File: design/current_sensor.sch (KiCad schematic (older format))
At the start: 10 parts, among them J1 DS conn, J2 DS conn, J3 Conn, J4 DS conn, U1 Buffer

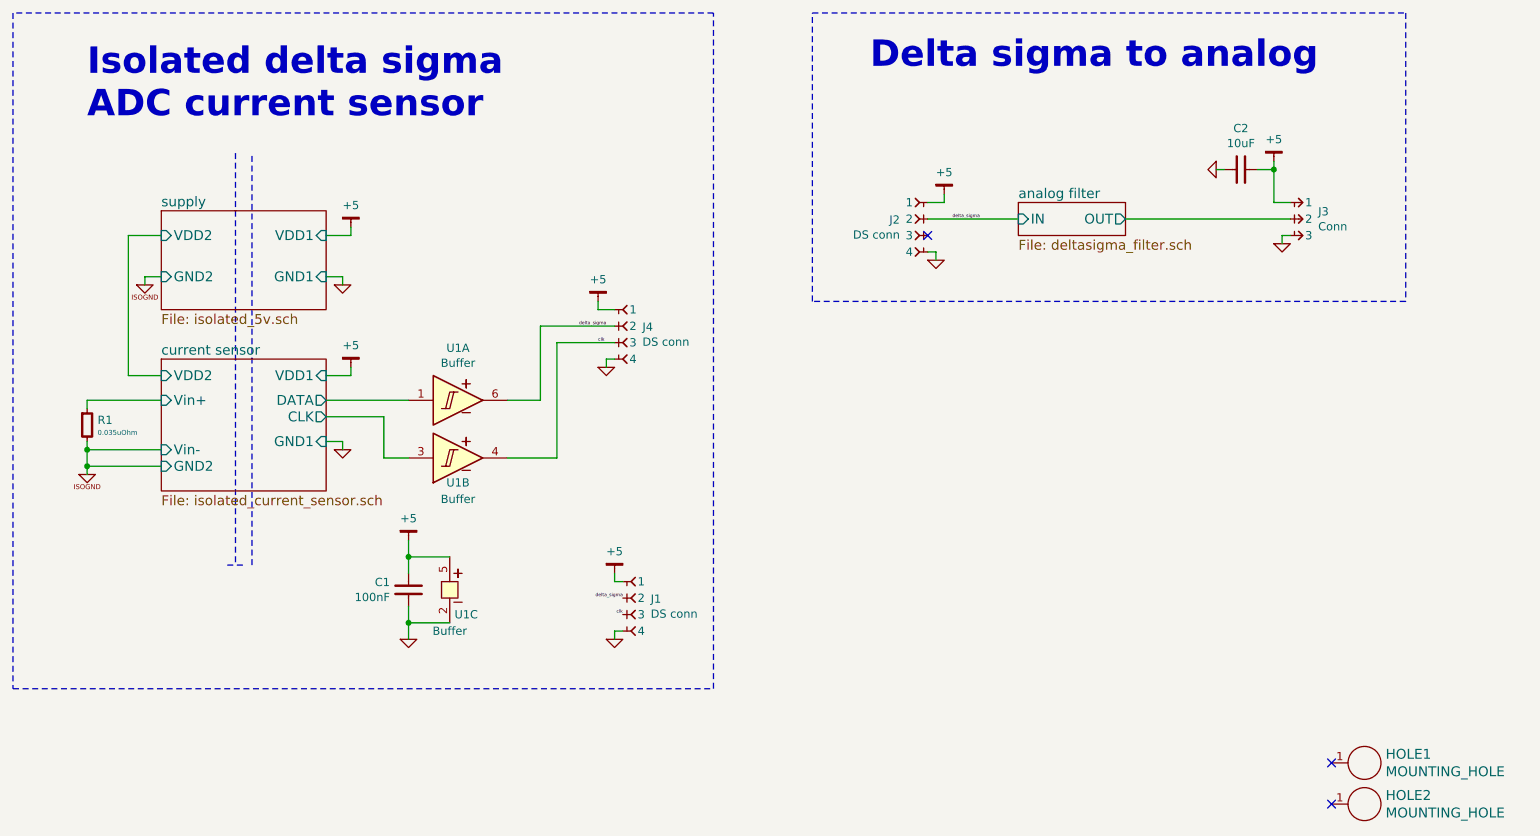
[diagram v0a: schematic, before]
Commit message: Added buffer to restore signal before opamp analog filter
Signed-off-by: Marcos Chaparro <mchaparro@paltatech.com>
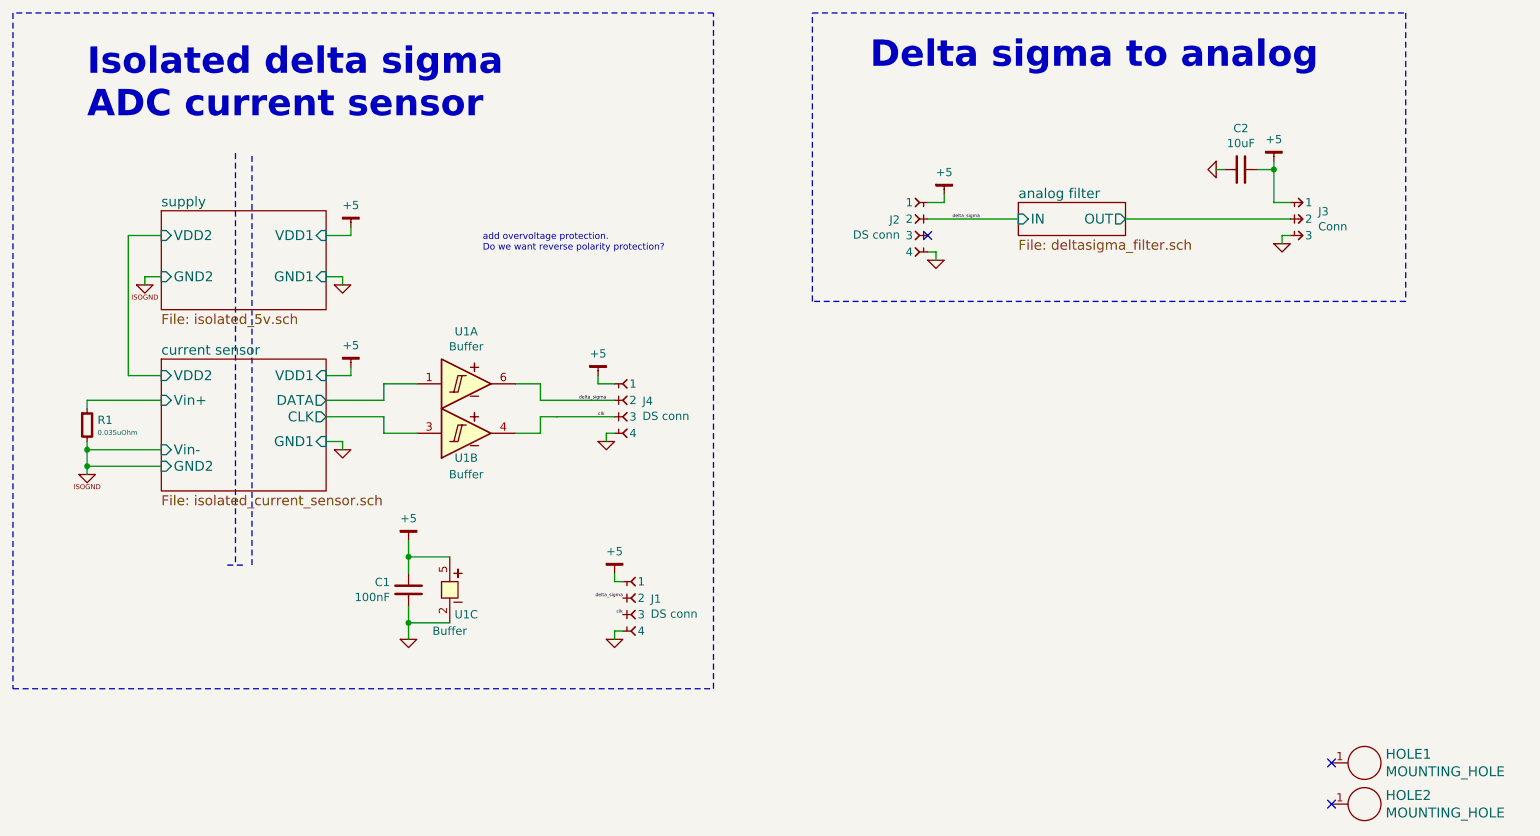
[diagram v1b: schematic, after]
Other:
- note added: "add overvoltage protection.\nDo we want reverse polarity protection?"
- moved on the sheet: J4, U1A, U1B
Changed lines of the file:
@@
 	2850 4150 2400 4150
 Wire Wire Line
-	2400 4100 2400 4300
+	2400 4100 2400 4150
+Wire Wire Line
+	2400 4150 2400 4250
+Wire Wire Line
+	2400 4250 2400 4300
 Wire Wire Line
 	2400 3850 2400 3900
@@
 L CONN-100MIL-F-1x4 J4
 U 1 1 59900007
-P 5650 3300
-F 0 "J4" H 5769 3195 50  0000 L CNN
-F 1 "DS conn" H 5769 3104 50  0000 L CNN
-F 2 "paltatech:DF13-4P-1.25H(50)" H 5650 3300 50  0001 C CNN
-F 3 "" H 5650 3300 50  0000 C CNN
-F 4 "DF13-4P-1.25H(50)" H 5650 3300 60  0001 C CNN "MPN"
-F 5 "0" H 5650 3300 60  0001 C CNN "Exclude from BOM"
-	1    5650 3300
-	1    0    0    -1
-$EndComp
-Wire Wire Line
-	5500 3300 5600 3300
+P 5650 3750
+F 0 "J4" H 5769 3645 50  0000 L CNN
+F 1 "DS conn" H 5769 3554 50  0000 L CNN
+F 2 "paltatech:DF13-4P-1.25H(50)" H 5650 3750 50  0001 C CNN
+F 3 "" H 5650 3750 50  0000 C CNN
+F 4 "DF13-4P-1.25H(50)" H 5650 3750 60  0001 C CNN "MPN"
+F 5 "0" H 5650 3750 60  0001 C CNN "Exclude from BOM"
+	1    5650 3750
+	1    0    0    -1
+$EndComp
+Wire Wire Line
+	5500 3750 5600 3750
 $Comp
 L GND #PWR01
 U 1 1 59900562
-P 5550 3650
-F 0 "#PWR01" H 5550 3650 30  0001 C CNN
-F 1 "GND" H 5550 3580 30  0001 C CNN
-F 2 "" H 5550 3650 60  0000 C CNN
-F 3 "" H 5550 3650 60  0000 C CNN
-	1    5550 3650
-	1    0    0    -1
-$EndComp
-Wire Wire Line
-	5550 3650 5550 3600
-Wire Wire Line
-	5550 3600 5600 3600
+P 5550 4100
+F 0 "#PWR01" H 5550 4100 30  0001 C CNN
+F 1 "GND" H 5550 4030 30  0001 C CNN
+F 2 "" H 5550 4100 60  0000 C CNN
+F 3 "" H 5550 4100 60  0000 C CNN
+	1    5550 4100
+	1    0    0    -1
+$EndComp
+Wire Wire Line
+	5550 4100 5550 4050
+Wire Wire Line
+	5550 4050 5600 4050
 $Comp
 L GND #PWR02
@@
 L BUF-Schmitt-Dual U1
 U 1 1 59901584
-P 4650 3850
-F 0 "U1" H 4650 4167 50  0000 C CNN
-F 1 "Buffer" H 4650 4076 50  0000 C CNN
-F 2 "smd-semi:SOT-23-6" H 4650 2850 50  0001 C CNN
-F 3 "datasheet" H 4650 2750 50  0001 C CNN
-F 4 "SN74LVC2G17DBVR" H 4750 4250 60  0001 C CNN "MPN"
-F 5 "0" H 4650 3850 60  0001 C CNN "Exclude from BOM"
-F 6 "bom" H 4650 2650 50  0001 C CNN "BOM"
-	1    4650 3850
+P 4700 3750
+F 0 "U1" H 4700 4067 50  0000 C CNN
+F 1 "Buffer" H 4700 3976 50  0000 C CNN
+F 2 "smd-semi:SOT-23-6" H 4700 2750 50  0001 C CNN
+F 3 "datasheet" H 4700 2650 50  0001 C CNN
+F 4 "SN74LVC2G17DBVR" H 4800 4150 60  0001 C CNN "MPN"
+F 5 "0" H 4700 3750 60  0001 C CNN "Exclude from BOM"
+F 6 "bom" H 4700 2550 50  0001 C CNN "BOM"
+	1    4700 3750
 	1    0    0    -1
 $EndComp
@@
 L BUF-Schmitt-Dual U1
 U 2 1 59901616
-P 4650 4200
-F 0 "U1" H 4650 4050 50  0000 C CNN
-F 1 "Buffer" H 4650 3950 50  0000 C CNN
-F 2 "smd-semi:SOT-23-6" H 4650 3200 50  0001 C CNN
-F 3 "datasheet" H 4650 3100 50  0001 C CNN
-F 4 "SN74LVC2G17DBVR" H 4750 4600 60  0001 C CNN "MPN"
-F 5 "0" H 4650 4200 60  0001 C CNN "Exclude from BOM"
-F 6 "bom" H 4650 3000 50  0001 C CNN "BOM"
-	2    4650 4200
+P 4700 4050
+F 0 "U1" H 4700 3900 50  0000 C CNN
+F 1 "Buffer" H 4700 3800 50  0000 C CNN
+F 2 "smd-semi:SOT-23-6" H 4700 3050 50  0001 C CNN
+F 3 "datasheet" H 4700 2950 50  0001 C CNN
+F 4 "SN74LVC2G17DBVR" H 4800 4450 60  0001 C CNN "MPN"
+F 5 "0" H 4700 4050 60  0001 C CNN "Exclude from BOM"
+F 6 "bom" H 4700 2850 50  0001 C CNN "BOM"
+	2    4700 4050
 	1    0    0    -1
 $EndComp
@@
 	4600 4800 4350 4800
 Wire Wire Line
-	4350 4700 4350 4900
+	4350 4700 4350 4800
+Wire Wire Line
+	4350 4800 4350 4900
 Wire Wire Line
 	4600 5200 4350 5200
 Wire Wire Line
-	4350 5100 4350 5300
-Wire Wire Line
-	4350 3850 3850 3850
+	4350 5100 4350 5200
+Wire Wire Line
+	4350 5200 4350 5300
 Wire Wire Line
 	3850 3950 4200 3950
 Wire Wire Line
-	4200 3950 4200 4200
-Wire Wire Line
-	4200 4200 4350 4200
-Wire Wire Line
-	4950 3850 5150 3850
-Wire Wire Line
-	5150 3850 5150 3400
-Wire Wire Line
-	5150 3400 5600 3400
-Wire Wire Line
-	5600 3500 5250 3500
-Wire Wire Line
-	5250 3500 5250 4200
-Wire Wire Line
-	5250 4200 4950 4200
+	4200 3950 4200 4050
+Wire Wire Line
+	5150 3750 5150 3850
+Wire Wire Line
+	5150 3850 5600 3850
+Wire Wire Line
+	5150 3950 5250 3950
+Wire Wire Line
+	5250 3950 5600 3950
 $Comp
 L CONN-100MIL-F-1x4 J2
@@
 L +5 #PWR04
 U 1 1 59903345
-P 5500 3250
-F 0 "#PWR04" H 5500 3300 30  0001 C CNN
-F 1 "+5" H 5500 3383 50  0000 C CNN
-F 2 "" H 5500 3250 60  0000 C CNN
-F 3 "" H 5500 3250 60  0000 C CNN
-	1    5500 3250
-	1    0    0    -1
-$EndComp
-Wire Wire Line
-	5500 3250 5500 3300
+P 5500 3700
+F 0 "#PWR04" H 5500 3750 30  0001 C CNN
+F 1 "+5" H 5500 3833 50  0000 C CNN
+F 2 "" H 5500 3700 60  0000 C CNN
+F 3 "" H 5500 3700 60  0000 C CNN
+	1    5500 3700
+	1    0    0    -1
+$EndComp
+Wire Wire Line
+	5500 3700 5500 3750
 $Comp
 L +5 #PWR05
@@
 	9500 2450 9600 2450
 Wire Wire Line
-	9600 2400 9600 2650
+	9600 2400 9600 2450
+Wire Wire Line
+	9600 2450 9600 2650
 Wire Wire Line
 	9600 2650 9700 2650
@@
 Text Label 5650 5150 2    20   ~ 0
 clk
-Text Label 5500 3500 0    20   ~ 0
+Text Label 5500 3950 0    20   ~ 0
 clk
-Text Label 5550 3400 2    20   ~ 0
+Text Label 5550 3850 2    20   ~ 0
 delta_sigma
 $Comp
@@
 	6800 3250 6800 1500
 $Comp
-L +5 #PWR?
+L +5 #PWR015
 U 1 1 599340FA
 P 4000 3650
-F 0 "#PWR?" H 4000 3700 30  0001 C CNN
+F 0 "#PWR015" H 4000 3700 30  0001 C CNN
 F 1 "+5" H 4000 3783 50  0000 C CNN
 F 2 "" H 4000 3650 60  0000 C CNN
@@
 	4000 3700 3850 3700
 $Comp
-L +5 #PWR?
+L +5 #PWR024
 U 1 1 599341EE
 P 4000 2800
-F 0 "#PWR?" H 4000 2850 30  0001 C CNN
+F 0 "#PWR024" H 4000 2850 30  0001 C CNN
 F 1 "+5" H 4000 2933 50  0000 C CNN
 F 2 "" H 4000 2800 60  0000 C CNN
@@
 Wire Wire Line
 	4000 2850 3850 2850
+Wire Wire Line
+	4200 4050 4400 4050
+Wire Wire Line
+	4200 3850 4200 3750
+Wire Wire Line
+	4200 3750 4400 3750
+Wire Wire Line
+	4200 3850 3850 3850
+Wire Wire Line
+	5000 3750 5150 3750
+Wire Wire Line
+	5150 3950 5150 4050
+Wire Wire Line
+	5150 4050 5000 4050
+Text Notes 4800 2950 0    40   ~ 0
+add overvoltage protection.\nDo we want reverse polarity protection?
 $EndSCHEMATC

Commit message: Added harness fault protections
Signed-off-by: Marcos Chaparro <mchaparro@paltatech.com>
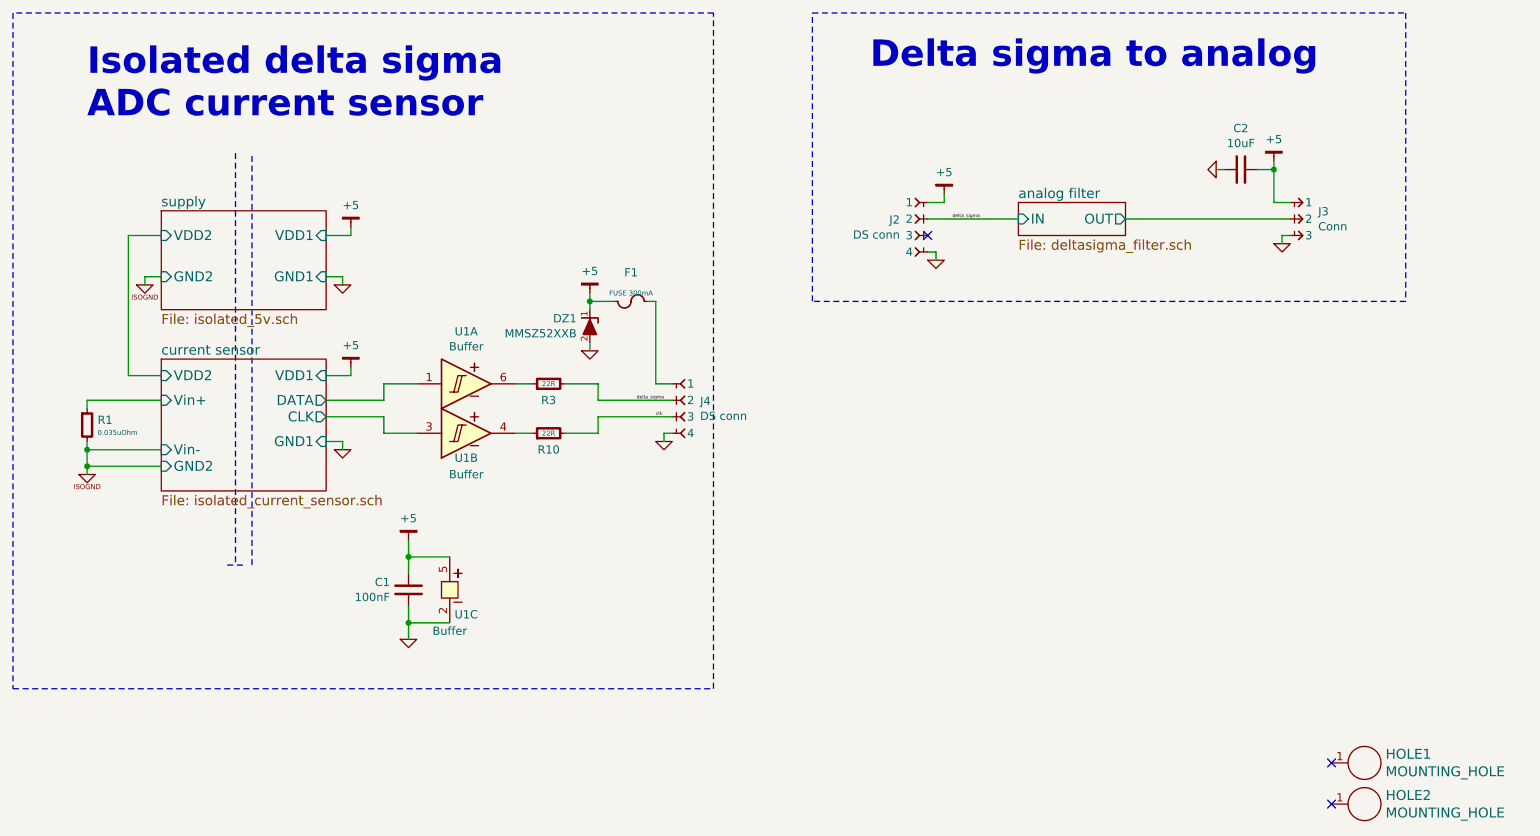
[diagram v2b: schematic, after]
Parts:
- removed J1: DS conn, conn-100mil:CONN-100MIL-F-1x4, symbol CONN-100MIL-F-1x4
- added DZ1: MMSZ52XXB, smd-semi:SOD-123, symbol MMSZ52XXB
- added F1: FUSE 300mA, IPC7351-Nominal:RESC2012X50, symbol FUSE
- added R10, R3: 22R, IPC7351-Nominal:RESC1608X50, symbol R-0603
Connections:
- net +5: now also DZ1.1 (K), F1.2; no longer J4.1
- net GND: now also DZ1.2 (A)
- net clk: now also R10.2; no longer U1.4 (2Y)
- net delta_sigma: now also R3.2; no longer U1.6 (1Y)
- new net: F1.1, J4.1
- new net: R3.1, U1.6 (1Y)
- new net: R10.1, U1.4 (2Y)
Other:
- note removed: "add overvoltage protection.\nDo we want reverse polarity protection?"
- moved on the sheet: J4
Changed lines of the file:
@@
 	2850 4150 2400 4150
 Wire Wire Line
-	2400 4100 2400 4150
-Wire Wire Line
-	2400 4150 2400 4250
-Wire Wire Line
-	2400 4250 2400 4300
+	2400 4100 2400 4300
 Wire Wire Line
 	2400 3850 2400 3900
@@
 L CONN-100MIL-F-1x4 J4
 U 1 1 59900007
-P 5650 3750
-F 0 "J4" H 5769 3645 50  0000 L CNN
-F 1 "DS conn" H 5769 3554 50  0000 L CNN
-F 2 "paltatech:DF13-4P-1.25H(50)" H 5650 3750 50  0001 C CNN
-F 3 "" H 5650 3750 50  0000 C CNN
-F 4 "DF13-4P-1.25H(50)" H 5650 3750 60  0001 C CNN "MPN"
-F 5 "0" H 5650 3750 60  0001 C CNN "Exclude from BOM"
-	1    5650 3750
-	1    0    0    -1
-$EndComp
-Wire Wire Line
-	5500 3750 5600 3750
+P 6000 3750
+F 0 "J4" H 6119 3645 50  0000 L CNN
+F 1 "DS conn" H 6119 3554 50  0000 L CNN
+F 2 "paltatech:DF13-4P-1.25H(50)" H 6000 3750 50  0001 C CNN
+F 3 "" H 6000 3750 50  0000 C CNN
+F 4 "DF13-4P-1.25H(50)" H 6000 3750 60  0001 C CNN "MPN"
+F 5 "0" H 6000 3750 60  0001 C CNN "Exclude from BOM"
+	1    6000 3750
+	1    0    0    -1
+$EndComp
+Wire Wire Line
+	5850 3750 5950 3750
 $Comp
 L GND #PWR01
 U 1 1 59900562
-P 5550 4100
-F 0 "#PWR01" H 5550 4100 30  0001 C CNN
-F 1 "GND" H 5550 4030 30  0001 C CNN
-F 2 "" H 5550 4100 60  0000 C CNN
-F 3 "" H 5550 4100 60  0000 C CNN
-	1    5550 4100
-	1    0    0    -1
-$EndComp
-Wire Wire Line
-	5550 4100 5550 4050
-Wire Wire Line
-	5550 4050 5600 4050
+P 5900 4100
+F 0 "#PWR01" H 5900 4100 30  0001 C CNN
+F 1 "GND" H 5900 4030 30  0001 C CNN
+F 2 "" H 5900 4100 60  0000 C CNN
+F 3 "" H 5900 4100 60  0000 C CNN
+	1    5900 4100
+	1    0    0    -1
+$EndComp
+Wire Wire Line
+	5900 4100 5900 4050
+Wire Wire Line
+	5900 4050 5950 4050
 $Comp
 L GND #PWR02
@@
 	4600 4800 4350 4800
 Wire Wire Line
-	4350 4700 4350 4800
-Wire Wire Line
-	4350 4800 4350 4900
+	4350 4700 4350 4900
 Wire Wire Line
 	4600 5200 4350 5200
 Wire Wire Line
-	4350 5100 4350 5200
-Wire Wire Line
-	4350 5200 4350 5300
+	4350 5100 4350 5300
 Wire Wire Line
 	3850 3950 4200 3950
@@
 	4200 3950 4200 4050
 Wire Wire Line
-	5150 3750 5150 3850
-Wire Wire Line
-	5150 3850 5600 3850
-Wire Wire Line
-	5150 3950 5250 3950
-Wire Wire Line
-	5250 3950 5600 3950
+	5500 3750 5500 3850
+Wire Wire Line
+	5500 3850 5950 3850
+Wire Wire Line
+	5500 3950 5950 3950
 $Comp
 L CONN-100MIL-F-1x4 J2
@@
 L +5 #PWR04
 U 1 1 59903345
-P 5500 3700
-F 0 "#PWR04" H 5500 3750 30  0001 C CNN
-F 1 "+5" H 5500 3833 50  0000 C CNN
-F 2 "" H 5500 3700 60  0000 C CNN
-F 3 "" H 5500 3700 60  0000 C CNN
-	1    5500 3700
-	1    0    0    -1
-$EndComp
-Wire Wire Line
-	5500 3700 5500 3750
+P 5450 3200
+F 0 "#PWR04" H 5450 3250 30  0001 C CNN
+F 1 "+5" H 5450 3333 50  0000 C CNN
+F 2 "" H 5450 3200 60  0000 C CNN
+F 3 "" H 5450 3200 60  0000 C CNN
+	1    5450 3200
+	1    0    0    -1
+$EndComp
+Wire Wire Line
+	5850 3250 5850 3750
 $Comp
 L +5 #PWR05
@@
 	9500 2450 9600 2450
 Wire Wire Line
-	9600 2400 9600 2450
-Wire Wire Line
-	9600 2450 9600 2650
+	9600 2400 9600 2650
 Wire Wire Line
 	9600 2650 9700 2650
@@
 	9650 2850 9700 2850
 NoConn ~ 7500 2850
-Text Label 5650 5050 2    20   ~ 0
-delta_sigma
 Text Label 7650 2750 0    20   ~ 0
 delta_sigma
@@
 $EndComp
 Connection ~ 4350 4800
-$Comp
-L CONN-100MIL-F-1x4 J1
-U 1 1 599101E9
-P 5700 4950
-F 0 "J1" H 5819 4845 50  0000 L CNN
-F 1 "DS conn" H 5819 4754 50  0000 L CNN
-F 2 "conn-100mil:CONN-100MIL-F-1x4" H 5700 4950 50  0001 C CNN
-F 3 "" H 5700 4950 50  0000 C CNN
-F 4 "0" H 5700 4950 60  0001 C CNN "Exclude from BOM"
-F 5 "none" H 5700 4950 60  0001 C CNN "version"
-	1    5700 4950
-	1    0    0    -1
-$EndComp
-$Comp
-L GND #PWR018
-U 1 1 599103D9
-P 5600 5300
-F 0 "#PWR018" H 5600 5300 30  0001 C CNN
-F 1 "GND" H 5600 5230 30  0001 C CNN
-F 2 "" H 5600 5300 60  0000 C CNN
-F 3 "" H 5600 5300 60  0000 C CNN
-	1    5600 5300
-	1    0    0    -1
-$EndComp
-Wire Wire Line
-	5600 5300 5600 5250
-Wire Wire Line
-	5600 5250 5650 5250
-$Comp
-L +5 #PWR019
-U 1 1 599104B9
-P 5600 4900
-F 0 "#PWR019" H 5600 4950 30  0001 C CNN
-F 1 "+5" H 5600 5033 50  0000 C CNN
-F 2 "" H 5600 4900 60  0000 C CNN
-F 3 "" H 5600 4900 60  0000 C CNN
-	1    5600 4900
-	1    0    0    -1
-$EndComp
-Wire Wire Line
-	5600 4900 5600 4950
-Wire Wire Line
-	5600 4950 5650 4950
-Text Label 5650 5150 2    20   ~ 0
+Text Label 5850 3950 0    20   ~ 0
 clk
-Text Label 5500 3950 0    20   ~ 0
-clk
-Text Label 5550 3850 2    20   ~ 0
+Text Label 5900 3850 2    20   ~ 0
 delta_sigma
 $Comp
@@
 	4200 3850 3850 3850
 Wire Wire Line
-	5000 3750 5150 3750
-Wire Wire Line
-	5150 3950 5150 4050
-Wire Wire Line
-	5150 4050 5000 4050
-Text Notes 4800 2950 0    40   ~ 0
-add overvoltage protection.\nDo we want reverse polarity protection?
+	5500 3950 5500 4050
+$Comp
+L R-0603 R?
+U 1 1 599DA554
+P 5200 3750
+AR Path="/589CF239/599DA554" Ref="R?"  Part="1"
+AR Path="/589B4343/599DA554" Ref="R?"  Part="1"
+AR Path="/589D1961/599DA554" Ref="R?"  Part="1"
+AR Path="/589D4558/599DA554" Ref="R?"  Part="1"
+AR Path="/598FD705/599DA554" Ref="R?"  Part="1"
+AR Path="/599DA554" Ref="R3"  Part="1"
+F 0 "R3" V 5100 3750 50  0000 C CNN
+F 1 "22R" V 5200 3750 30  0000 C CNN
+F 2 "IPC7351-Nominal:RESC1608X50" H 5200 3750 50  0001 C CNN
+F 3 "" H 5200 3800 60  0001 C CNN
+F 4 "0" H 5200 3750 60  0001 C CNN "Exclude from BOM"
+F 5 "RES SMD 1k 5% [0603]" H 5950 4300 60  0001 C CNN "BOM"
+F 6 "Yageo" H 500 -500 50  0001 C CNN "MFR"
+F 7 "Digikey" H 500 -500 50  0001 C CNN "SPR"
+	1    5200 3750
+	0    -1   -1   0
+$EndComp
+Wire Wire Line
+	5100 3750 5000 3750
+Wire Wire Line
+	5300 3750 5500 3750
+$Comp
+L R-0603 R?
+U 1 1 599DA7B8
+P 5200 4050
+AR Path="/589CF239/599DA7B8" Ref="R?"  Part="1"
+AR Path="/589B4343/599DA7B8" Ref="R?"  Part="1"
+AR Path="/589D1961/599DA7B8" Ref="R?"  Part="1"
+AR Path="/589D4558/599DA7B8" Ref="R?"  Part="1"
+AR Path="/598FD705/599DA7B8" Ref="R?"  Part="1"
+AR Path="/599DA7B8" Ref="R10"  Part="1"
+F 0 "R10" V 5100 4050 50  0000 C CNN
+F 1 "22R" V 5200 4050 30  0000 C CNN
+F 2 "IPC7351-Nominal:RESC1608X50" H 5200 4050 50  0001 C CNN
+F 3 "" H 5200 4100 60  0001 C CNN
+F 4 "0" H 5200 4050 60  0001 C CNN "Exclude from BOM"
+F 5 "RES SMD 1k 5% [0603]" H 5950 4600 60  0001 C CNN "BOM"
+F 6 "Yageo" H 500 -200 50  0001 C CNN "MFR"
+F 7 "Digikey" H 500 -200 50  0001 C CNN "SPR"
+	1    5200 4050
+	0    -1   -1   0
+$EndComp
+Wire Wire Line
+	5500 4050 5300 4050
+Wire Wire Line
+	5100 4050 5000 4050
+$Comp
+L FUSE F1
+U 1 1 599DB09F
+P 5700 3250
+F 0 "F1" V 5525 3250 50  0000 C CNN
+F 1 "FUSE 300mA" V 5650 3250 30  0000 C CNN
+F 2 "IPC7351-Nominal:RESC2012X50" V 5577 3250 60  0001 C CNN
+F 3 "" H 5700 3300 60  0000 C CNN
+F 4 "0ZCK0010FF2G" H 5700 3250 60  0001 C CNN "MPN"
+F 5 "0" H 5700 3250 60  0001 C CNN "Exclude from BOM"
+	1    5700 3250
+	0    1    1    0
+$EndComp
+Wire Wire Line
+	5450 3200 5450 3300
+Wire Wire Line
+	5450 3250 5600 3250
+Wire Wire Line
+	5800 3250 5850 3250
+$Comp
+L MMSZ52XXB DZ1
+U 1 1 599DB8C8
+P 5450 3400
+F 0 "DZ1" H 5530 3446 50  0000 L CNN
+F 1 "MMSZ52XXB" H 5530 3355 50  0000 L CNN
+F 2 "smd-semi:SOD-123" H 5450 3250 50  0001 C CNN
+F 3 "" H 5450 3400 60  0000 C CNN
+	1    5450 3400
+	-1   0    0    -1
+$EndComp
+Connection ~ 5450 3250
+$Comp
+L GND #PWR018
+U 1 1 599DBAE6
+P 5450 3550
+F 0 "#PWR018" H 5450 3550 30  0001 C CNN
+F 1 "GND" H 5450 3480 30  0001 C CNN
+F 2 "" H 5450 3550 60  0000 C CNN
+F 3 "" H 5450 3550 60  0000 C CNN
+	1    5450 3550
+	1    0    0    -1
+$EndComp
+Wire Wire Line
+	5450 3550 5450 3500
 $EndSCHEMATC
